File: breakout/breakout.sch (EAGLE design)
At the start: 241 parts, among them J15 1789472, J16 1789472, J27 69168-124HLF, J30 SJ1-3514-SMT-TR, J32 69168-116HLF, J33 12226-8250-00FR, J34 1888276, J35 69168-116HLF, J36 1888276, Q1 SI1012R, Q2 SI1012R, Q3 SI1012R, Q4 SI1012R, Q5 SI1012R, Q6 SI1012R, Q7 SI1012R, Q8 SI1012R, U1 SK6805-E-J, U10 TXB0101, U11 SK6805-E-J, U12 SK6805-E-J, U13 SK6805-E-J, U14 SK6805-E-J, U15 SK6805-E-J, U16 SK6805-E-J, U17 SK6805-E-J, U18 SK6805-E-J, U19 SK6805-E-J, U2 SK6805-E-J, U20 SK6805-E-J, U21 SK6805-E-J, U22 SK6805-E-J, U23 SK6805-E-J, U24 SK6805-E-J, U25 SK6805-E-J, U26 SK6805-E-J, U27 SK6805-E-J, U28 SK6805-E-J, U29 SK6805-E-J, U3 SK6805-E-J, U30 SK6805-E-J, U31 SK6805-E-J, U32 SK6805-E-J, U33 SK6805-E-J, U34 SK6805-E-J, U35 SK6805-E-J, U36 SK6805-E-J, U37 SK6805-E-J, U38 SK6805-E-J, U39 SK6805-E-J, U4 SK6805-E-J, U40 SK6805-E-J, U41 SK6805-E-J, U42 SK6805-E-J, U43 G6K-2F-RF, U44 G6K-2F-RF, U45 G6K-2F-RF, U46 G6K-2F-RF, U47 LTM4622A, U48 SI8610, U49 TINY-FPGA-BX, U5 SK6805-E-J, U50 TCA9555, U51 FIN1032MTCX, U52 SN65LVDS9638DGN, U53 SN65LVDS9638DGN, U6 SK6805-E-J, U7 SK6805-E-J, U8 SK6805-E-J, U9 SK6805-E-J

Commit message: Changes to breakout rev 1.4 after case fit test with rev 1.3
- Moved components to prevent them from being smashed by case
- More clearance around M3 holes
- Smaller font on analog BNC labels
- Moved the terminal blocks so that there spacing makes more sense for
related signals.
- Modeled screw terminal blocks correctly
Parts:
- removed TP8: (no value), jonnew:TPTP19R
- R11: value 13.3k -> 1k
- R12: value 649k -> 100k
- R13: value 8.25k -> 1k
- R14, R16: value 4.7k -> 100k
- R15: value 4.7k -> 1k
- R17: value 100 -> 1k
- R18: value 100 -> 100k
- R19: value 270, 0.5W -> 13.3k; device jonnew:R_0805 -> jonnew:R_0402
- R20: value 270, 0.5W -> 649k; device jonnew:R_0805 -> jonnew:R_0402
- R21: value 270, 0.5W -> 8.25k; device jonnew:R_0805 -> jonnew:R_0402
- R22, R23, R24: value 270, 0.5W -> 4.7k; device jonnew:R_0805 -> jonnew:R_0402
- R25, R26: value 270, 0.5W -> 100; device jonnew:R_0805 -> jonnew:R_0402
- R35, R37, R39, R41: value 100k -> 270, 0.5W; device jonnew:R_0402 -> jonnew:R_0805
- R36, R38, R40, R42: value 1k -> 270, 0.5W; device jonnew:R_0402 -> jonnew:R_0805
- TP7: device jonnew:TP_2MM -> jonnew:TPTP19R
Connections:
- net !TCA_INT: now also R22.2; no longer R14.2
- net +12V: now also TP7.TP; no longer TP8.TP
- net +3V3: now also R22.1, R23.1, R24.1; no longer R14.1, R15.1, R16.1
- net AGND: now also TP6.TP; no longer TP7.TP
- net BUTTON0: now also S5.P; no longer S6.P
- net BUTTON1: now also S7.P; no longer S8.P
- net BUTTON2: now also S9.P; no longer S10.P
- net BUTTON3: now also S6.P; no longer S5.P
- net BUTTON4: now also S8.P; no longer S7.P
- net BUTTON5: now also S10.P; no longer S9.P
- net DIN0: now also R42.2; no longer R34.2
- net DIN0_P: now also R42.1; no longer R34.1
- net DIN1: now also R34.2; no longer R26.2
- net DIN1_P: now also R34.1; no longer R26.1
- net DIN2: now also R40.2; no longer R32.2
- net DIN2_P: now also R40.1; no longer R32.1
- net DIN3: now also R32.2; no longer R24.2
- net DIN3_P: now also R32.1; no longer R24.1
- net DIN4: now also R38.2; no longer R30.2
- net DIN4_P: now also R38.1; no longer R30.1
- net DIN5: now also R30.2; no longer R22.2
- net DIN5_P: now also R30.1; no longer R22.1
- net DIN6: now also R36.2; no longer R28.2
- net DIN6_P: now also R36.1; no longer R28.1
- net DIN7: now also R28.2; no longer R20.2
- net DIN7_P: now also R28.1; no longer R20.1
- net DOUT0: now also D21.CH2, R27.2; no longer D21.CH8, R19.2
- net DOUT0_P: now also R27.1; no longer R19.1
- net DOUT1: now also D21.CH1, R29.2; no longer D21.CH7, R21.2
- net DOUT1_P: now also R29.1; no longer R21.1
- net DOUT2: now also D21.CH3, R31.2; no longer D21.CH2, R23.2
- net DOUT2_P: now also R31.1; no longer R23.1
- net DOUT3: now also D21.CH4, R33.2; no longer D21.CH6, R25.2
- net DOUT3_P: now also R33.1; no longer R25.1
- net DOUT4: now also D21.CH8, R35.2; no longer D21.CH3, R27.2
- net DOUT4_P: now also R35.1; no longer R27.1
- net DOUT5: now also D21.CH7, R37.2; no longer D21.CH5, R29.2
- net DOUT5_P: now also R37.1; no longer R29.1
- net DOUT6: now also D21.CH6, R39.2; no longer D21.CH4, R31.2
- net DOUT6_P: now also R39.1; no longer R31.1
- net DOUT7: now also D21.CH5, R41.2; no longer D21.CH1, R33.2
- net DOUT7_P: now also R41.1; no longer R33.1
- net GND: now also R11.1, R12.1, R13.1, R14.1, R15.1, R16.1, R17.1, R18.1, R19.2, R20.2, R21.2; no longer R11.2, R12.2, R13.2, R35.1, R36.1, R37.1, R38.1, R39.1, R40.1, R41.1, R42.1, TP6.TP
- net I2C_SCL: now also R23.2; no longer R15.2
- net I2C_SDA: now also R24.2; no longer R16.2
- net LVDS_DOUT0_N: now also R25.1; no longer R17.1
- net LVDS_DOUT0_P: now also R25.2; no longer R17.2
- net LVDS_DOUT1_N: now also R26.1; no longer R18.1
- net LVDS_DOUT1_P: now also R26.2; no longer R18.2
- net N$145: now also R20.1; no longer R12.1
- net N$24: now also R21.1; no longer R13.1
- net N$25: now also R19.1; no longer R11.1
- net RELAY_AND_0: now also R11.2; no longer R36.2
- net RELAY_AND_1: now also R13.2; no longer R38.2
- net RELAY_AND_2: now also R15.2; no longer R40.2
- net RELAY_AND_3: now also R17.2; no longer R42.2
- net RELAY_MECH_0: now also R12.2; no longer R35.2
- net RELAY_MECH_1: now also R14.2; no longer R37.2
- net RELAY_MECH_2: now also R16.2; no longer R39.2
- net RELAY_MECH_3: now also R18.2; no longer R41.2
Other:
- moved on the sheet: R11, R12, R13, R14, R15, R16, R17, R18, R19, R20, R21, R22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

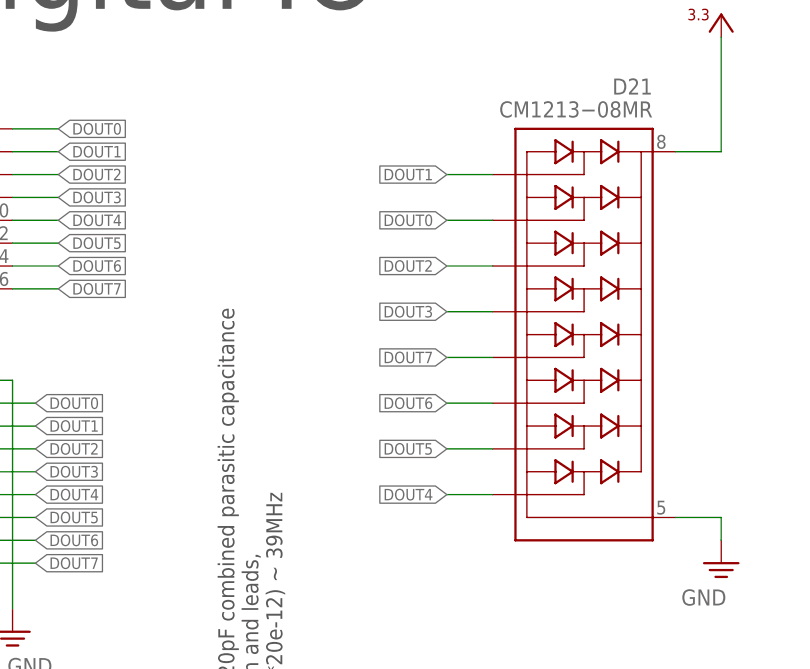
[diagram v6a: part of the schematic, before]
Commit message: Minore updates to breakout rev 1.4
- Address issues found during the construction of the case
- DOUT IDC and terminal block switch positions to match the other two IO
banks
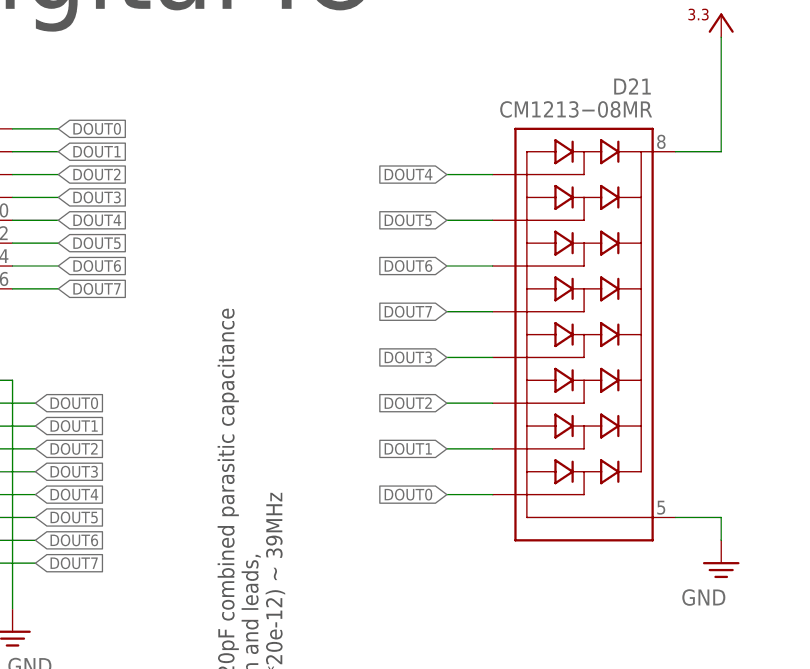
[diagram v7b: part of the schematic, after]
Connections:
- net DOUT0: now also D21.CH8; no longer D21.CH2
- net DOUT1: now also D21.CH7; no longer D21.CH1
- net DOUT2: now also D21.CH6; no longer D21.CH3
- net DOUT3: now also D21.CH5; no longer D21.CH4
- net DOUT4: now also D21.CH1; no longer D21.CH8
- net DOUT5: now also D21.CH2; no longer D21.CH7
- net DOUT6: now also D21.CH3; no longer D21.CH6
- net DOUT7: now also D21.CH4; no longer D21.CH5
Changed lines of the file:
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@@
 </segment>
 <segment>
-<wire x1="401.32" y1="132.08" x2="396.24" y2="132.08" width="0.1524" layer="91"/>
-<label x="396.24" y="132.08" size="1.27" layer="95" rot="MR0" xref="yes"/>
-<pinref part="D21" gate="G$1" pin="CH2"/>
+<wire x1="401.32" y1="101.6" x2="396.24" y2="101.6" width="0.1524" layer="91"/>
+<label x="396.24" y="101.6" size="1.27" layer="95" rot="MR0" xref="yes"/>
+<pinref part="D21" gate="G$1" pin="CH8"/>
 </segment>
 </net>
@@
 </segment>
 <segment>
-<wire x1="401.32" y1="137.16" x2="396.24" y2="137.16" width="0.1524" layer="91"/>
-<label x="396.24" y="137.16" size="1.27" layer="95" rot="MR0" xref="yes"/>
-<pinref part="D21" gate="G$1" pin="CH1"/>
+<wire x1="401.32" y1="106.68" x2="396.24" y2="106.68" width="0.1524" layer="91"/>
+<label x="396.24" y="106.68" size="1.27" layer="95" rot="MR0" xref="yes"/>
+<pinref part="D21" gate="G$1" pin="CH7"/>
 </segment>
 </net>
@@
 </segment>
 <segment>
-<wire x1="401.32" y1="127" x2="396.24" y2="127" width="0.1524" layer="91"/>
-<label x="396.24" y="127" size="1.27" layer="95" rot="MR0" xref="yes"/>
-<pinref part="D21" gate="G$1" pin="CH3"/>
+<wire x1="401.32" y1="111.76" x2="396.24" y2="111.76" width="0.1524" layer="91"/>
+<label x="396.24" y="111.76" size="1.27" layer="95" rot="MR0" xref="yes"/>
+<pinref part="D21" gate="G$1" pin="CH6"/>
 </segment>
 </net>
@@
 </segment>
 <segment>
-<wire x1="401.32" y1="121.92" x2="396.24" y2="121.92" width="0.1524" layer="91"/>
-<label x="396.24" y="121.92" size="1.27" layer="95" rot="MR0" xref="yes"/>
-<pinref part="D21" gate="G$1" pin="CH4"/>
+<wire x1="401.32" y1="116.84" x2="396.24" y2="116.84" width="0.1524" layer="91"/>
+<label x="396.24" y="116.84" size="1.27" layer="95" rot="MR0" xref="yes"/>
+<pinref part="D21" gate="G$1" pin="CH5"/>
 </segment>
 </net>
@@
 </segment>
 <segment>
-<wire x1="401.32" y1="101.6" x2="396.24" y2="101.6" width="0.1524" layer="91"/>
-<label x="396.24" y="101.6" size="1.27" layer="95" rot="MR0" xref="yes"/>
-<pinref part="D21" gate="G$1" pin="CH8"/>
+<wire x1="401.32" y1="137.16" x2="396.24" y2="137.16" width="0.1524" layer="91"/>
+<label x="396.24" y="137.16" size="1.27" layer="95" rot="MR0" xref="yes"/>
+<pinref part="D21" gate="G$1" pin="CH1"/>
 </segment>
 </net>
@@
 </segment>
 <segment>
-<wire x1="401.32" y1="106.68" x2="396.24" y2="106.68" width="0.1524" layer="91"/>
-<label x="396.24" y="106.68" size="1.27" layer="95" rot="MR0" xref="yes"/>
-<pinref part="D21" gate="G$1" pin="CH7"/>
+<wire x1="401.32" y1="132.08" x2="396.24" y2="132.08" width="0.1524" layer="91"/>
+<label x="396.24" y="132.08" size="1.27" layer="95" rot="MR0" xref="yes"/>
+<pinref part="D21" gate="G$1" pin="CH2"/>
 </segment>
 </net>
@@
 </segment>
 <segment>
-<wire x1="401.32" y1="111.76" x2="396.24" y2="111.76" width="0.1524" layer="91"/>
-<label x="396.24" y="111.76" size="1.27" layer="95" rot="MR0" xref="yes"/>
-<pinref part="D21" gate="G$1" pin="CH6"/>
+<wire x1="401.32" y1="127" x2="396.24" y2="127" width="0.1524" layer="91"/>
+<label x="396.24" y="127" size="1.27" layer="95" rot="MR0" xref="yes"/>
+<pinref part="D21" gate="G$1" pin="CH3"/>
 </segment>
 </net>
@@
 </segment>
 <segment>
-<wire x1="401.32" y1="116.84" x2="396.24" y2="116.84" width="0.1524" layer="91"/>
-<label x="396.24" y="116.84" size="1.27" layer="95" rot="MR0" xref="yes"/>
-<pinref part="D21" gate="G$1" pin="CH5"/>
+<wire x1="401.32" y1="121.92" x2="396.24" y2="121.92" width="0.1524" layer="91"/>
+<label x="396.24" y="121.92" size="1.27" layer="95" rot="MR0" xref="yes"/>
+<pinref part="D21" gate="G$1" pin="CH4"/>
 </segment>
 </net>

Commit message: More updates to breakout rev. 1.4 to fit case
- Swiched 2x 8 pin screw terminals for a single 16 pin screw terminal.
- Moved m3 clearance holes in front of IDC connectors up a bit
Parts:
- removed J36: 1888276, jonnew:PINHD-1X9_SCREW2
- J15: value 1789472 -> (none); device jonnew:SCREW8_2 -> jonnew:COAX_MMCX-THRU
- J16: value 1789472 -> (none); device jonnew:SCREW8_2 -> jonnew:COAX_SMA-VERT
- J17: value (none) -> 1789074; device jonnew:COAX_MMCX-THRU -> jonnew:PINHD-1X16
- J18: device jonnew:COAX_SMA-VERT -> jonnew:COAX_MMCX-THRU
- J19, J28: device jonnew:COAX_MMCX-THRU -> jonnew:COAX_SMA-VERT
- J20: device jonnew:COAX_SMA-VERT -> jonnew:COAX_0731010360
- J26: value (none) -> 69168-124HLF; device jonnew:COAX_0731010360 -> jonnew:PINHD-2X12_0.1"
- J27: value 69168-124HLF -> (none); device jonnew:PINHD-2X12_0.1" -> jonnew:COAX_MMCX-THRU
- J29: value (none) -> SJ1-3514-SMT-TR; device jonnew:COAX_SMA-VERT -> jonnew:STEREO_JACK
- J30: value SJ1-3514-SMT-TR -> (none); device jonnew:STEREO_JACK -> jonnew:JP2E_THRU-HOLE
- J31: value (none) -> 69168-116HLF; device jonnew:JP2E_THRU-HOLE -> jonnew:PINHD-2X8_THRU
- J32: value 69168-116HLF -> 12226-8250-00FR; device jonnew:PINHD-2X8_THRU -> jonnew:PINHD-1X26_122
- J33: value 12226-8250-00FR -> 1888276; device jonnew:PINHD-1X26_122 -> jonnew:PINHD-1X9_SCREW2
- J34: value 1888276 -> 69168-116HLF; device jonnew:PINHD-1X9_SCREW2 -> jonnew:PINHD-2X8_THRU
- J35: value 69168-116HLF -> 1888276; device jonnew:PINHD-2X8_THRU -> jonnew:PINHD-1X9_SCREW2
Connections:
- net +12V: now also J32.1, J32.26; no longer J33.1, J33.26
- net AGND: now also J17.1, J17.15, J17.16, J17.2, J20.2, J26.1, J26.11, J26.13, J26.15, J26.17, J26.19, J26.21, J26.23, J26.3, J26.5, J26.7, J26.9, J32.13, J32.14; no longer J15.1, J15.2, J16.1, J16.2, J26.2, J27.1, J27.11, J27.13, J27.15, J27.17, J27.19, J27.21, J27.23, J27.3, J27.5, J27.7, J27.9, J33.13, J33.14
- net AIO_0: now also J17.3, J26.2, J32.20; no longer J15.3, J27.2, J33.20
- net AIO_1: now also J17.4, J26.4, J32.7; no longer J15.4, J27.4, J33.7
- net AIO_10: now also J17.13, J24.1, J26.22, J32.15; no longer J16.7, J25.1, J27.22, J33.15
- net AIO_11: now also J17.14, J25.1, J26.24, J32.2; no longer J16.8, J26.1, J27.24, J33.2
- net AIO_2: now also J17.5, J26.6, J32.19; no longer J15.5, J27.6, J33.19
- net AIO_3: now also J17.6, J26.8, J32.6; no longer J15.6, J27.8, J33.6
- net AIO_4: now also J17.7, J26.10, J32.18; no longer J15.7, J27.10, J33.18
- net AIO_5: now also J17.8, J26.12, J32.5; no longer J15.8, J27.12, J33.5
- net AIO_6: now also J17.9, J20.1, J26.14, J32.17; no longer J16.3, J21.1, J27.14, J33.17
- net AIO_7: now also J17.10, J21.1, J26.16, J32.4; no longer J16.4, J22.1, J27.16, J33.4
- net AIO_8: now also J17.11, J22.1, J26.18, J32.16; no longer J16.5, J23.1, J27.18, J33.16
- net AIO_9: now also J17.12, J23.1, J26.20, J32.3; no longer J16.6, J24.1, J27.20, J33.3
- net DIN0: now also J34.2; no longer J36.2
- net DIN1: now also J34.4, J35.3; no longer J35.4, J36.3
- net DIN2: now also J34.6, J35.4; no longer J35.6, J36.4
- net DIN3: now also J34.8, J35.5; no longer J35.8, J36.5
- net DIN4: now also J34.10, J35.6; no longer J35.10, J36.6
- net DIN5: now also J34.12, J35.7; no longer J35.12, J36.7
- net DIN6: now also J34.14, J35.8; no longer J35.14, J36.8
- net DIN7: now also J34.16, J35.9; no longer J35.16, J36.9
- net DOUT0: now also J31.2, J33.2; no longer J32.2, J34.2
- net DOUT1: now also J31.4, J33.3; no longer J32.4, J34.3
- net DOUT2: now also J31.6, J33.4; no longer J32.6, J34.4
- net DOUT3: now also J31.8, J33.5; no longer J32.8, J34.5
- net DOUT4: now also J31.10, J33.6; no longer J32.10, J34.6
- net DOUT5: now also J31.12, J33.7; no longer J32.12, J34.7
- net DOUT6: now also J31.14, J33.8; no longer J32.14, J34.8
- net DOUT7: now also J31.16, J33.9; no longer J32.16, J34.9
- net GND: now also J15.2, J16.2, J27.2, J30.2, J31.1, J31.11, J31.13, J31.15, J31.3, J31.5, J31.7, J31.9, J32.PAD1, J32.PAD2, J33.1, J34.11, J34.13, J34.15, J34.3, J34.5, J34.7, J34.9; no longer J17.2, J20.2, J29.2, J31.2, J32.1, J32.11, J32.13, J32.15, J32.3, J32.5, J32.7, J32.9, J33.PAD1, J33.PAD2, J35.11, J35.13, J35.15, J35.3, J35.5, J35.7, J35.9, J36.1
- net LVDS_DIN0_N: now also J32.23; no longer J33.23
- net LVDS_DIN0_P: now also J32.10; no longer J33.10
- net LVDS_DIN1_N: now also J32.11; no longer J33.11
- net LVDS_DIN1_P: now also J32.24; no longer J33.24
- net LVDS_DIN2_N: now also J32.25; no longer J33.25
- net LVDS_DIN2_P: now also J32.12; no longer J33.12
- net LVDS_DOUT0_N: now also J32.8; no longer J33.8
- net LVDS_DOUT0_P: now also J32.21; no longer J33.21
- net LVDS_DOUT1_N: now also J32.9; no longer J33.9
- net LVDS_DOUT1_P: now also J32.22; no longer J33.22
- net N$1: now also J15.1, J16.1; no longer J17.1, J18.1
- net N$16: now also J29.1; no longer J30.1
- net N$17: now also J29.5; no longer J30.5
- net N$18: now also J29.4; no longer J30.4
- net N$3: now also J18.1; no longer J20.1
- net N$4: now also J27.1; no longer J29.1
- net NEOPIXEL_DIN: now also J30.1; no longer J31.1
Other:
- moved on the sheet: J18, J19, J20, J21, J22, J23, J24, J25, J28
